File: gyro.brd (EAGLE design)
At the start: 27.8 x 16.1 mm, 12 parts, among them IC3 FXAS21002C

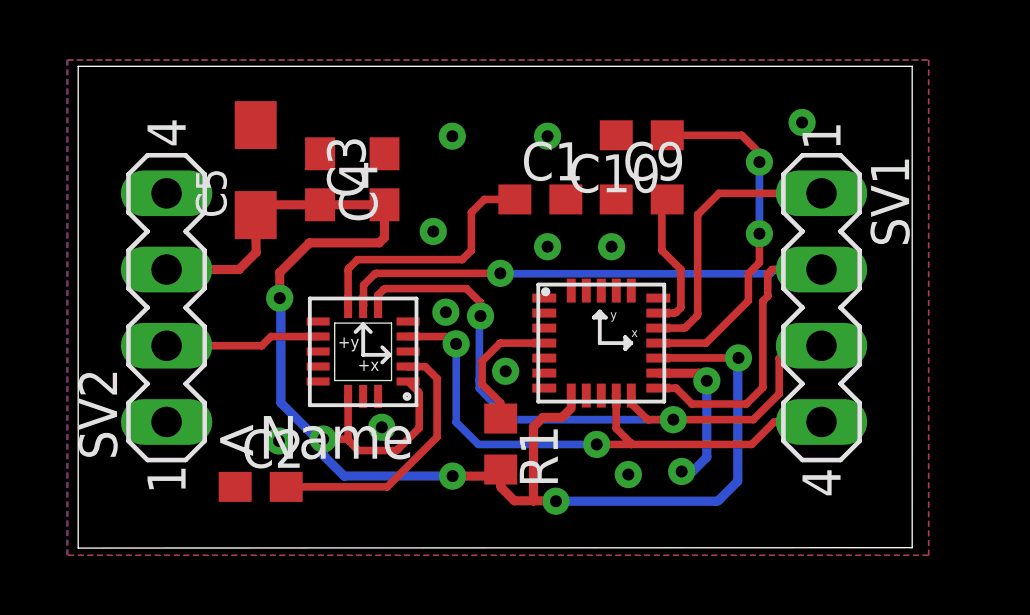
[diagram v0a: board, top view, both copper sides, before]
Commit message: INT_A i dopasowanie goldpinow
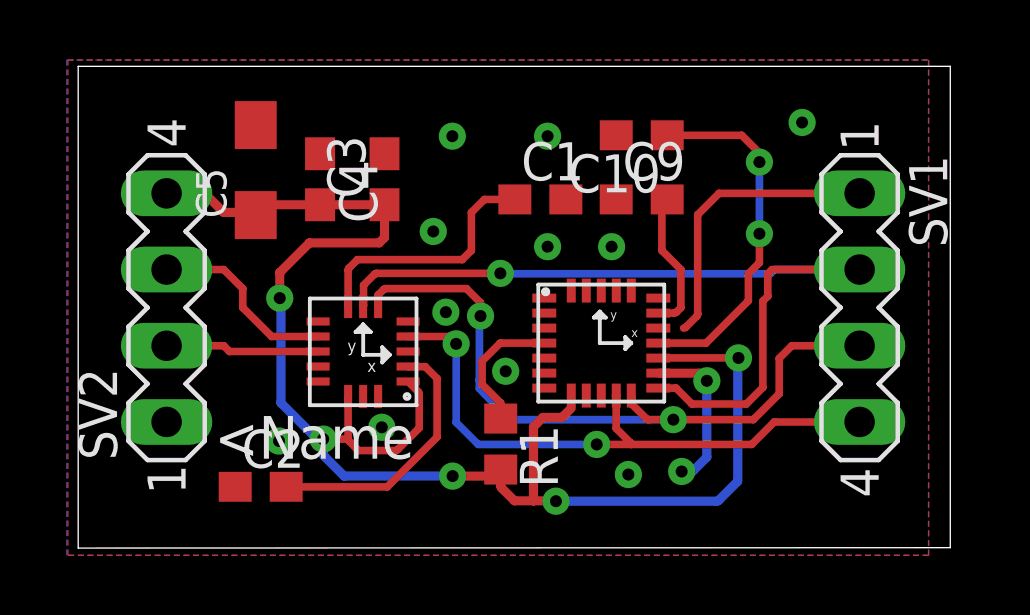
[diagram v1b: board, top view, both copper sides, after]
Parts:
- moved SV1 1.27 mm to (28.2, 94.6)
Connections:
- net CS_B renamed CS_G
- net N$28 renamed INT_G
- removed net NONE: SV2.4
- net +3V3: now also SV2.4; no longer SV2.3
- net CS_A: now also SV2.3; no longer SV2.2
- net INT_A: now also SV2.2
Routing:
- net INT_A: track 0.00 -> 5.13 mm
- net MISO: track 25.8 -> 28.4 mm
- net SCLK: track 19.0 -> 20.3 mm
- net MOSI: track 22.5 -> 23.8 mm
- net +3V3: track 54.1 -> 52.9 mm
- net CS_A: track 5.18 -> 6.35 mm
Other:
- board size 27.8 x 16.1 mm -> 29.1 x 16.1 mm
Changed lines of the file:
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@@
 <board>
 <plain>
-<wire x1="2.1336" y1="86.6013" x2="29.9332" y2="86.614" width="0" layer="20"/>
-<wire x1="29.9332" y1="86.614" x2="29.9332" y2="102.659" width="0" layer="20"/>
-<wire x1="29.9332" y1="102.659" x2="2.1336" y2="102.659" width="0" layer="20"/>
+<wire x1="2.1336" y1="86.6013" x2="31.2032" y2="86.614" width="0" layer="20"/>
+<wire x1="31.2032" y1="86.614" x2="31.2032" y2="102.659" width="0" layer="20"/>
+<wire x1="31.2032" y1="102.659" x2="2.1336" y2="102.659" width="0" layer="20"/>
 <wire x1="2.1336" y1="102.659" x2="2.1336" y2="86.6013" width="0" layer="20"/>
 </plain>
@@
 <element name="IC3" library="_microMouse" package="QFN24-4X4" value="FXAS21002C" x="19.5199" y="93.4339"/>
 <element name="U$2" library="_microMouse" package="QFN16-5X3" value="FXOS8700CQR1" x="11.6332" y="93.1418" rot="R180"/>
-<element name="SV1" library="con-lstb" package="MA04-1" value="" x="26.9113" y="94.615" rot="R270">
-<attribute name="OC_NEWARK" value="unknown" x="26.9113" y="94.615" size="1.778" layer="27" rot="R270" display="off"/>
-<attribute name="MPN" value="" x="26.9113" y="94.615" size="1.778" layer="27" rot="R270" display="off"/>
-<attribute name="MF" value="" x="26.9113" y="94.615" size="1.778" layer="27" rot="R270" display="off"/>
-<attribute name="OC_FARNELL" value="unknown" x="26.9113" y="94.615" size="1.778" layer="27" rot="R270" display="off"/>
+<element name="SV1" library="con-lstb" package="MA04-1" value="" x="28.1813" y="94.615" rot="R270">
+<attribute name="OC_NEWARK" value="unknown" x="28.1813" y="94.615" size="1.778" layer="27" rot="R270" display="off"/>
+<attribute name="MPN" value="" x="28.1813" y="94.615" size="1.778" layer="27" rot="R270" display="off"/>
+<attribute name="MF" value="" x="28.1813" y="94.615" size="1.778" layer="27" rot="R270" display="off"/>
+<attribute name="OC_FARNELL" value="unknown" x="28.1813" y="94.615" size="1.778" layer="27" rot="R270" display="off"/>
 </element>
 <element name="SV2" library="con-lstb" package="MA04-1" value="" x="5.08" y="94.615" rot="R90">
@@
 <wire x1="25.5016" y1="91.7448" x2="25.5016" y2="92.9259" width="0.254" layer="1"/>
 <wire x1="25.5016" y1="92.9259" x2="25.9207" y2="93.345" width="0.254" layer="1"/>
-<wire x1="25.9207" y1="93.345" x2="26.9113" y2="93.345" width="0.254" layer="1"/>
+<wire x1="25.9207" y1="93.345" x2="28.1813" y2="93.345" width="0.254" layer="1"/>
 </signal>
 <signal name="MISO">
@@
 <wire x1="22.0613" y1="91.9339" x2="22.5933" y2="91.4019" width="0.254" layer="1"/>
 <wire x1="25.205515625" y1="95.7453" x2="25.345215625" y2="95.885" width="0.254" layer="16"/>
-<wire x1="25.345215625" y1="95.885" x2="26.9113" y2="95.885" width="0.254" layer="16"/>
+<wire x1="25.345215625" y1="95.885" x2="28.1813" y2="95.885" width="0.254" layer="16"/>
 <wire x1="24.9555" y1="94.8309" x2="25.1206" y2="94.996" width="0.254" layer="1"/>
 <wire x1="25.1206" y1="94.996" x2="25.1206" y2="95.7453" width="0.254" layer="1"/>
 <wire x1="25.1206" y1="95.7453" x2="25.2603" y2="95.885" width="0.254" layer="1"/>
-<wire x1="25.2603" y1="95.885" x2="26.9113" y2="95.885" width="0.254" layer="1"/>
+<wire x1="25.2603" y1="95.885" x2="28.1813" y2="95.885" width="0.254" layer="1"/>
 <wire x1="22.5933" y1="91.4019" x2="24.405415625" y2="91.4019" width="0.254" layer="1"/>
 <wire x1="24.405415625" y1="91.4019" x2="24.9555" y2="91.951984375" width="0.254" layer="1"/>
@@
 <wire x1="20.574" y1="90.0557" x2="24.5872" y2="90.0557" width="0.254" layer="1"/>
 <wire x1="24.5872" y1="90.0557" x2="25.3365" y2="90.805" width="0.254" layer="1"/>
-<wire x1="25.3365" y1="90.805" x2="26.9113" y2="90.805" width="0.254" layer="1"/>
+<wire x1="25.3365" y1="90.805" x2="28.1813" y2="90.805" width="0.254" layer="1"/>
 </signal>
 <signal name="INT_A">
 <contactref element="U$2" pad="P$11"/>
+<contactref element="SV2" pad="2"/>
+<wire x1="10.1302" y1="93.1528" x2="7.1772" y2="93.1528" width="0.254" layer="1"/>
+<wire x1="7.1772" y1="93.1528" x2="6.985" y2="93.345" width="0.254" layer="1"/>
+<wire x1="6.985" y1="93.345" x2="5.08" y2="93.345" width="0.254" layer="1"/>
 </signal>
 <signal name="+3V3">
@@
 <contactref element="C4" pad="2"/>
 <contactref element="U$2" pad="P$14"/>
-<contactref element="SV2" pad="3"/>
+<contactref element="SV2" pad="4"/>
 <contactref element="R1" pad="2"/>
 <contactref element="IC3" pad="VDD"/>
@@
 <wire x1="12.1666" y1="96.774" x2="12.3444" y2="96.9518" width="0.3048" layer="1"/>
 <wire x1="12.3444" y1="96.9518" x2="12.3444" y2="98.0449" width="0.3048" layer="1"/>
-<wire x1="5.08" y1="95.885" x2="7.493" y2="95.885" width="0.3048" layer="1"/>
-<wire x1="8.0518" y1="97.6997" x2="8.0645" y2="96.4565" width="0.3048" layer="1"/>
-<wire x1="8.0645" y1="96.4565" x2="7.493" y2="95.885" width="0.3048" layer="1"/>
+<wire x1="5.08" y1="98.425" x2="6.35" y2="98.425" width="0.3048" layer="1"/>
+<wire x1="6.35" y1="98.425" x2="6.985" y2="97.79" width="0.3048" layer="1"/>
+<wire x1="6.985" y1="97.79" x2="7.9615" y2="97.79" width="0.3048" layer="1"/>
+<wire x1="7.9615" y1="97.79" x2="8.0518" y2="97.6997" width="0.3048" layer="1"/>
 </signal>
 <signal name="VDDIO">
@@
 <wire x1="21.59" y1="96.52" x2="22.225" y2="95.885" width="0.254" layer="1"/>
 <wire x1="22.225" y1="95.885" x2="22.225" y2="94.615" width="0.254" layer="1"/>
-</signal>
-<signal name="CS_B">
-<contactref element="IC3" pad="SPI_CS_B"/>
-<contactref element="SV1" pad="1"/>
-<wire x1="21.4699" y1="93.9339" x2="22.314615625" y2="93.9339" width="0.254" layer="1"/>
-<wire x1="22.314615625" y1="93.9339" x2="22.386459375" y2="93.963659375" width="0.254" layer="1" curve="45.001246"/>
-<wire x1="22.386459375" y1="93.963659375" x2="22.754040625" y2="94.331240625" width="0.254" layer="1"/>
-<wire x1="22.754040625" y1="94.331240625" x2="22.7838" y2="94.403084375" width="0.254" layer="1" curve="45.001762"/>
-<wire x1="22.7838" y1="94.403084375" x2="22.7838" y2="97.7138" width="0.254" layer="1"/>
-<wire x1="26.9113" y1="98.425" x2="23.495" y2="98.425" width="0.254" layer="1"/>
-<wire x1="23.495" y1="98.425" x2="22.7838" y2="97.7138" width="0.254" layer="1"/>
 </signal>
 <signal name="N$26">
@@
 <contactref element="IC3" pad="PWR_CTRL"/>
 </signal>
-<signal name="N$28">
-<contactref element="IC3" pad="INT1"/>
-</signal>
 <signal name="N$30">
 <contactref element="IC3" pad="RST_B"/>
@@
 <wire x1="16.2179" y1="91.437459375" x2="16.2179" y2="90.9184" width="0.254" layer="1"/>
 </signal>
-<signal name="NONE">
-<contactref element="SV2" pad="4"/>
+<signal name="INT_G">
+<contactref element="IC3" pad="INT1"/>
 </signal>
 <signal name="CS_A">
 <contactref element="U$2" pad="P$10"/>
-<contactref element="SV2" pad="2"/>
-<wire x1="10.1302" y1="93.6528" x2="8.5628" y2="93.6528" width="0.254" layer="1"/>
-<wire x1="5.08" y1="93.345" x2="8.255" y2="93.345" width="0.254" layer="1"/>
-<wire x1="8.255" y1="93.345" x2="8.5628" y2="93.6528" width="0.254" layer="1"/>
+<contactref element="SV2" pad="3"/>
+<wire x1="5.08" y1="95.885" x2="6.985" y2="95.885" width="0.254" layer="1"/>
+<wire x1="6.985" y1="95.885" x2="7.62" y2="95.25" width="0.254" layer="1"/>
+<wire x1="7.62" y1="95.25" x2="7.62" y2="94.615" width="0.254" layer="1"/>
+<wire x1="10.1302" y1="93.6528" x2="8.5822" y2="93.6528" width="0.254" layer="1"/>
+<wire x1="8.5822" y1="93.6528" x2="7.62" y2="94.615" width="0.254" layer="1"/>
+</signal>
+<signal name="CS_G">
+<contactref element="IC3" pad="SPI_CS_B"/>
+<contactref element="SV1" pad="1"/>
+<wire x1="22.314615625" y1="93.9339" x2="22.386459375" y2="93.963659375" width="0.254" layer="1" curve="45.001246"/>
+<wire x1="22.386459375" y1="93.963659375" x2="22.754040625" y2="94.331240625" width="0.254" layer="1"/>
+<wire x1="22.754040625" y1="94.331240625" x2="22.7838" y2="94.403084375" width="0.254" layer="1" curve="45.001762"/>
+<wire x1="22.7838" y1="94.403084375" x2="22.7838" y2="97.7138" width="0.254" layer="1"/>
+<wire x1="28.1813" y1="98.425" x2="23.495" y2="98.425" width="0.254" layer="1"/>
+<wire x1="23.495" y1="98.425" x2="22.7838" y2="97.7138" width="0.254" layer="1"/>
+<wire x1="22.314615625" y1="93.9339" x2="21.4699" y2="93.9339" width="0" layer="19" extent="1-1"/>
 </signal>
 </signals>

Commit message: dodanie wymiarowania do gyro i zepsucie termali :P
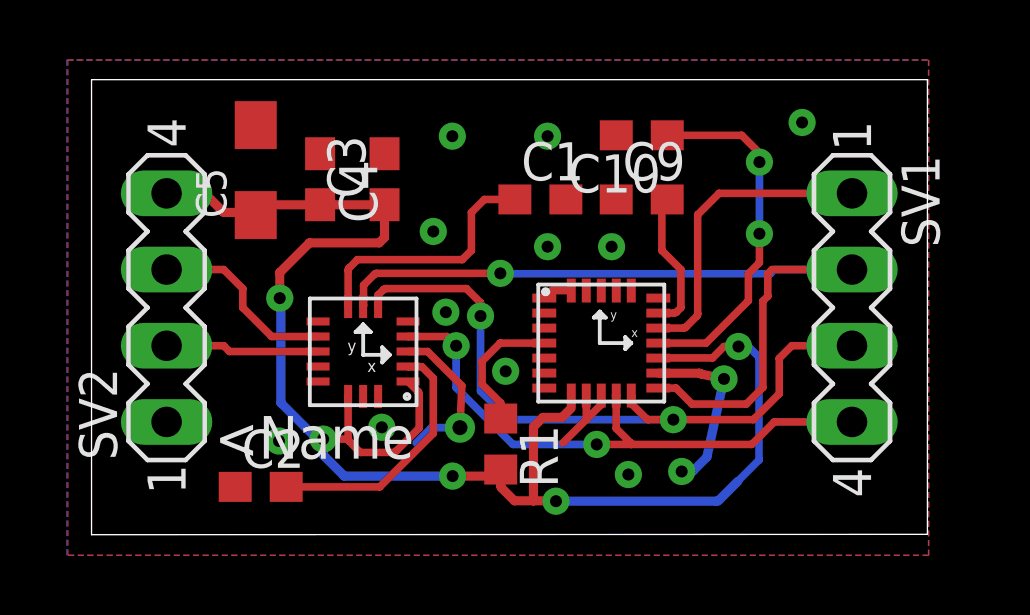
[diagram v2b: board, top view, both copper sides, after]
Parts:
- moved SV1 0.25 mm to (27.9, 94.6)
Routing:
- net GND: track 5.34 -> 15.3 mm, vias 13 -> 14
- net +3V3: track 52.9 -> 54.3 mm
- net SCLK: track 20.3 -> 19.4 mm
- net CS_G: track 9.68 -> 10.3 mm
- net MISO: track 28.4 -> 27.9 mm
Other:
- board size 29.1 x 16.1 mm -> 27.9 x 15.2 mm

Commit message: drobna aktualizacja
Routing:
- net MISO: track 27.9 -> 26.9 mm
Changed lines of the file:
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@@
 <dimension x1="5.08" y1="90.805" x2="2.54" y2="90.8685" x3="3.81" y3="83.439" textsize="1.778" layer="47" dtype="horizontal" unit="mil" visible="yes"/>
 <dimension x1="27.94" y1="90.805" x2="30.48" y2="90.805" x3="29.21" y3="83.6295" textsize="1.778" layer="47" dtype="horizontal" unit="mil" visible="yes"/>
-<dimension x1="2.6035" y1="102.235" x2="30.48" y2="102.87" x3="16.54175" y3="102.87" textsize="1.778" layer="47" dtype="horizontal" unit="mil" visible="yes"/>
+<dimension x1="2.54" y1="102.235" x2="30.48" y2="102.87" x3="16.51" y3="102.87" textsize="1.778" layer="47" dtype="horizontal" unit="mil" visible="yes"/>
 <dimension x1="2.5781" y1="102.2145" x2="30.4412" y2="102.2145" x3="16.50965" y3="106.4895" textsize="1.778" layer="47" dtype="horizontal" visible="yes"/>
 </plain>
@@
 <wire x1="16.2052" y1="95.758" x2="16.235859375" y2="95.7453" width="0.254" layer="16" curve="45"/>
 <wire x1="16.235859375" y1="95.7453" x2="25.205515625" y2="95.7453" width="0.254" layer="16"/>
-<wire x1="24.9555" y1="91.951984375" x2="24.9555" y2="94.8309" width="0.254" layer="1"/>
 <wire x1="21.4699" y1="91.9339" x2="22.0613" y2="91.9339" width="0.254" layer="1"/>
 <wire x1="22.0613" y1="91.9339" x2="22.5933" y2="91.4019" width="0.254" layer="1"/>
 <wire x1="25.205515625" y1="95.7453" x2="25.345215625" y2="95.885" width="0.254" layer="16"/>
 <wire x1="25.345215625" y1="95.885" x2="27.9273" y2="95.885" width="0.254" layer="16"/>
-<wire x1="24.9555" y1="94.8309" x2="25.1206" y2="94.996" width="0.254" layer="1"/>
-<wire x1="25.1206" y1="94.996" x2="25.1206" y2="95.7453" width="0.254" layer="1"/>
-<wire x1="25.1206" y1="95.7453" x2="25.2603" y2="95.885" width="0.254" layer="1"/>
-<wire x1="25.2603" y1="95.885" x2="27.9273" y2="95.885" width="0.254" layer="1"/>
 <wire x1="22.5933" y1="91.4019" x2="24.405415625" y2="91.4019" width="0.254" layer="1"/>
 <wire x1="24.405415625" y1="91.4019" x2="24.9555" y2="91.951984375" width="0.254" layer="1"/>
+<wire x1="24.9555" y1="91.951984375" x2="24.9555" y2="93.98" width="0.254" layer="1"/>
+<wire x1="24.9555" y1="93.98" x2="26.8605" y2="95.885" width="0.254" layer="1"/>
+<wire x1="26.8605" y1="95.885" x2="27.9273" y2="95.885" width="0.254" layer="1"/>
 </signal>
 <signal name="N$6">

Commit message: poprawilem poligon w gryo
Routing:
- net GND: track 15.3 -> 6.35 mm
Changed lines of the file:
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@@
 <setting verticaltext="up"/>
 </settings>
-<grid distance="2.5" unitdist="mil" unit="mil" style="lines" multiple="1" display="yes" altdistance="0.5" altunitdist="mil" altunit="mil"/>
+<grid distance="10" unitdist="mil" unit="mil" style="lines" multiple="1" display="yes" altdistance="0.5" altunitdist="mil" altunit="mil"/>
 <layers>
 <layer number="1" name="Top" color="4" fill="1" visible="yes" active="yes"/>
@@
 <param name="srMinRoundness" value="0mil"/>
 <param name="srMaxRoundness" value="0mil"/>
-<param name="slThermalIsolate" value="8mil"/>
+<param name="slThermalIsolate" value="6mil"/>
 <param name="slThermalsForVias" value="0"/>
 <param name="dpMaxLengthDifference" value="10mm"/>
@@
 <contactref element="C10" pad="2"/>
 <contactref element="U$2" pad="P$13"/>
-<via x="20.4724" y="89.0524" extent="1-16" drill="0.4"/>
+<via x="20.5105" y="89.1667" extent="1-16" drill="0.4"/>
 <via x="12.254" y="90.627" extent="1-16" drill="0.4"/>
 <via x="8.8265" y="90.17" extent="1-16" drill="0.4"/>
-<polygon width="0.2" layer="1" spacing="0.254" isolate="0.254">
+<polygon width="0.2" layer="1" spacing="0.254" isolate="0.2032">
 <vertex x="1.7907" y="102.87"/>
 <vertex x="30.48" y="102.87"/>
@@
 <via x="14.3891" y="94.4626" extent="1-16" drill="0.4"/>
 <via x="16.383" y="92.4941" extent="1-16" drill="0.4"/>
-<polygon width="0.254" layer="16">
+<polygon width="0.254" layer="16" isolate="0.2032">
 <vertex x="1.7526" y="102.87"/>
 <vertex x="30.48" y="102.87"/>
@@
 <contactref element="IC3" pad="GND3"/>
 <wire x1="21.4699" y1="92.4339" x2="21.477865625" y2="92.4306" width="0.254" layer="1" curve="45"/>
-<wire x1="21.477865625" y1="92.4306" x2="22.830615625" y2="92.4306" width="0.3048" layer="1"/>
-<wire x1="22.830615625" y1="92.4306" x2="22.902459375" y2="92.400840625" width="0.3048" layer="1" curve="-45.001246"/>
-<wire x1="22.902459375" y1="92.400840625" x2="23.6601" y2="92.2401" width="0.3048" layer="1"/>
 <via x="23.6601" y="92.2401" extent="1-16" drill="0.4"/>
-<wire x1="23.6601" y1="92.2401" x2="23.0886" y2="89.630684375" width="0.3048" layer="16"/>
-<wire x1="23.0886" y1="89.630684375" x2="22.641675" y2="89.183759375" width="0.3048" layer="16"/>
-<wire x1="22.641675" y1="89.183759375" x2="22.56983125" y2="89.154" width="0.3048" layer="16" curve="-45.001762"/>
-<wire x1="22.56983125" y1="89.154" x2="22.2504" y2="89.154" width="0.3048" layer="16"/>
-<via x="22.2504" y="89.154" extent="1-16" drill="0.4"/>
-<wire x1="22.2504" y1="89.154" x2="22.2123" y2="89.154" width="0.3048" layer="1"/>
-<wire x1="19.0699" y1="91.6839" x2="19.0699" y2="90.8884" width="0.254" layer="1"/>
-<wire x1="19.0699" y1="90.8884" x2="18.288" y2="90.1065" width="0.254" layer="1"/>
-<wire x1="19.0699" y1="90.8884" x2="19.558" y2="91.3765" width="0.254" layer="1"/>
-<wire x1="19.558" y1="91.3765" x2="19.558" y2="91.7575" width="0.254" layer="1"/>
-<wire x1="13.1302" y1="93.1528" x2="13.7812" y2="93.1528" width="0.254" layer="1"/>
-<wire x1="13.7812" y1="93.1528" x2="14.9225" y2="92.0115" width="0.254" layer="1"/>
-<wire x1="14.9225" y1="92.0115" x2="14.859" y2="90.6145" width="0.254" layer="1"/>
-<via x="14.859" y="90.6145" extent="1-16" drill="0.5" shape="octagon"/>
-<wire x1="14.859" y1="90.6145" x2="13.9065" y2="90.6145" width="0.254" layer="16"/>
-<wire x1="13.9065" y1="90.6145" x2="13.3985" y2="90.1065" width="0.254" layer="16"/>
-<wire x1="17.6699" y1="94.9339" x2="17.9199" y2="95.1839" width="0.254" layer="1"/>
-<wire x1="17.9199" y1="95.1839" x2="18.5699" y2="95.1839" width="0.254" layer="1"/>
+<wire x1="21.477865625" y1="92.4306" x2="23.4696" y2="92.4306" width="0.254" layer="1"/>
+<wire x1="23.4696" y1="92.4306" x2="23.6601" y2="92.2401" width="0.254" layer="1"/>
+<via x="22.2123" y="89.154" extent="1-16" drill="0.4"/>
+<wire x1="22.2123" y1="89.154" x2="22.8854" y2="89.154" width="0.254" layer="16"/>
+<wire x1="22.8854" y1="89.154" x2="23.6601" y2="89.9287" width="0.254" layer="16"/>
+<wire x1="23.6601" y1="89.9287" x2="23.6601" y2="92.2401" width="0.254" layer="16"/>
+<via x="25.5905" y="88.4047" extent="1-16" drill="0.4"/>
 </signal>
 <signal name="MOSI">
@@
 <contactref element="SV1" pad="3"/>
 <via x="21.971" y="90.8812" extent="1-16" drill="0.4"/>
-<wire x1="20.5699" y1="91.6839" x2="20.5867" y2="91.643340625" width="0.254" layer="1" curve="-45"/>
-<wire x1="20.5867" y1="91.643340625" x2="20.5867" y2="91.4019" width="0.254" layer="1"/>
-<wire x1="20.5867" y1="91.4019" x2="21.077640625" y2="90.910959375" width="0.254" layer="1"/>
-<wire x1="21.077640625" y1="90.910959375" x2="21.149484375" y2="90.8812" width="0.254" layer="1" curve="45.001762"/>
-<wire x1="21.149484375" y1="90.8812" x2="21.971" y2="90.8812" width="0.254" layer="1"/>
 <wire x1="21.971" y1="90.8812" x2="16.4973" y2="90.8812" width="0.254" layer="16"/>
 <wire x1="12.1302" y1="94.6528" x2="12.1285" y2="94.656903125" width="0.254" layer="1" curve="-45"/>
@@
 <wire x1="15.5448" y1="94.3356" x2="15.5448" y2="91.8337" width="0.254" layer="16"/>
 <wire x1="15.5448" y1="91.8337" x2="16.4973" y2="90.8812" width="0.254" layer="16"/>
+<wire x1="21.971" y1="90.8812" x2="20.8026" y2="90.8812" width="0.254" layer="1"/>
+<wire x1="20.8026" y1="90.8812" x2="20.574" y2="91.1098" width="0.254" layer="1"/>
+<wire x1="20.574" y1="91.1098" x2="20.574" y2="91.6798" width="0.254" layer="1"/>
+<wire x1="20.574" y1="91.6798" x2="20.5699" y2="91.6839" width="0.254" layer="1"/>
 </signal>
 <signal name="MISO">
@@
 <contactref element="SV1" pad="4"/>
 <wire x1="13.1302" y1="93.6528" x2="13.13744375" y2="93.6498" width="0.254" layer="1" curve="45"/>
-<wire x1="20.0699" y1="91.6839" x2="20.066" y2="91.674484375" width="0.3048" layer="1" curve="45"/>
 <wire x1="20.066" y1="91.674484375" x2="20.066" y2="90.5891" width="0.254" layer="1"/>
 <wire x1="20.066" y1="90.5891" x2="20.556040625" y2="90.099059375" width="0.254" layer="1"/>
@@
 <wire x1="16.6243" y1="90.0557" x2="14.732" y2="91.948" width="0.254" layer="16"/>
 <wire x1="14.732" y1="91.948" x2="14.732" y2="93.345" width="0.254" layer="16"/>
+<wire x1="20.066" y1="91.674484375" x2="20.0699" y2="91.6839" width="0" layer="19" extent="1-1"/>
 </signal>
 <signal name="INT_A">
@@
 <via x="8.8519" y="94.9325" extent="1-16" drill="0.4"/>
 <wire x1="8.8519" y1="94.9706" x2="8.8519" y2="94.9325" width="0.254" layer="1"/>
-<wire x1="8.8519" y1="94.9325" x2="8.89" y2="94.8944" width="0.254" layer="16"/>
-<wire x1="8.89" y1="94.8944" x2="8.89" y2="91.44" width="0.3048" layer="16"/>
-<wire x1="8.89" y1="91.44" x2="10.0965" y2="90.2335" width="0.3048" layer="16"/>
 <wire x1="10.0965" y1="90.2335" x2="10.2997" y2="90.2335" width="0.254" layer="16"/>
 <contactref element="IC3" pad="I2C_B/SPI"/>
@@
 <wire x1="23.2791" y1="92.9386" x2="23.6601" y2="93.3196" width="0.254" layer="1"/>
 <wire x1="23.6601" y1="93.3196" x2="24.1427" y2="93.3196" width="0.254" layer="1"/>
-<wire x1="24.1173" y1="88.8238" x2="24.8285" y2="89.535" width="0.254" layer="16"/>
-<wire x1="24.8285" y1="89.535" x2="24.8285" y2="92.964" width="0.254" layer="16"/>
-<wire x1="24.8285" y1="92.964" x2="24.4729" y2="93.3196" width="0.254" layer="16"/>
-<wire x1="24.4729" y1="93.3196" x2="24.1427" y2="93.3196" width="0.254" layer="16"/>
+<wire x1="24.1173" y1="88.8238" x2="24.8285" y2="89.535" width="0.3048" layer="16"/>
+<wire x1="24.8285" y1="89.535" x2="24.8285" y2="92.964" width="0.3048" layer="16"/>
+<wire x1="24.8285" y1="92.964" x2="24.4729" y2="93.3196" width="0.3048" layer="16"/>
+<wire x1="24.4729" y1="93.3196" x2="24.1427" y2="93.3196" width="0.3048" layer="16"/>
+<wire x1="10.0965" y1="90.2335" x2="8.8519" y2="91.4781" width="0.3048" layer="16"/>
+<wire x1="8.8519" y1="91.4781" x2="8.8519" y2="94.9325" width="0.3048" layer="16"/>
 </signal>
 <signal name="VDDIO">
